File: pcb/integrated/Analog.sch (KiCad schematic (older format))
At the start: 49 parts, among them J5001 Conn_Coaxial, U5001 74LVC1G3157GW, U5002 TLV3501AIDBVR, U5003 74LVC1G3157GW, U5004 MCP6561-OT

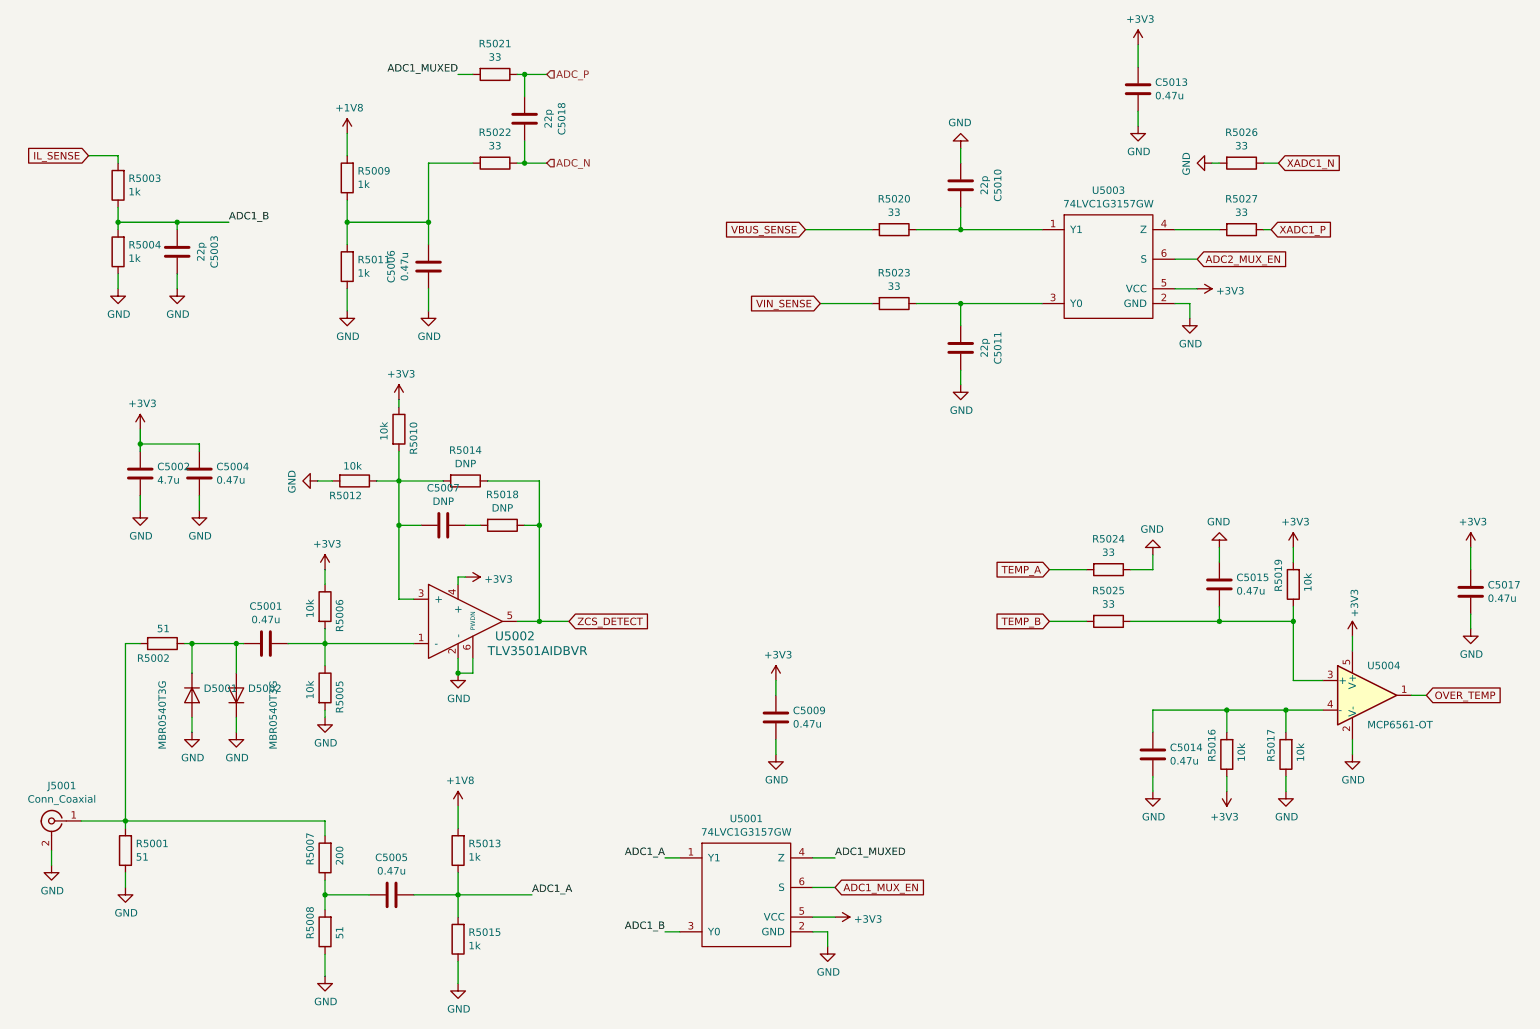
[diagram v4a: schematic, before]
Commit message: updated component values for schematic
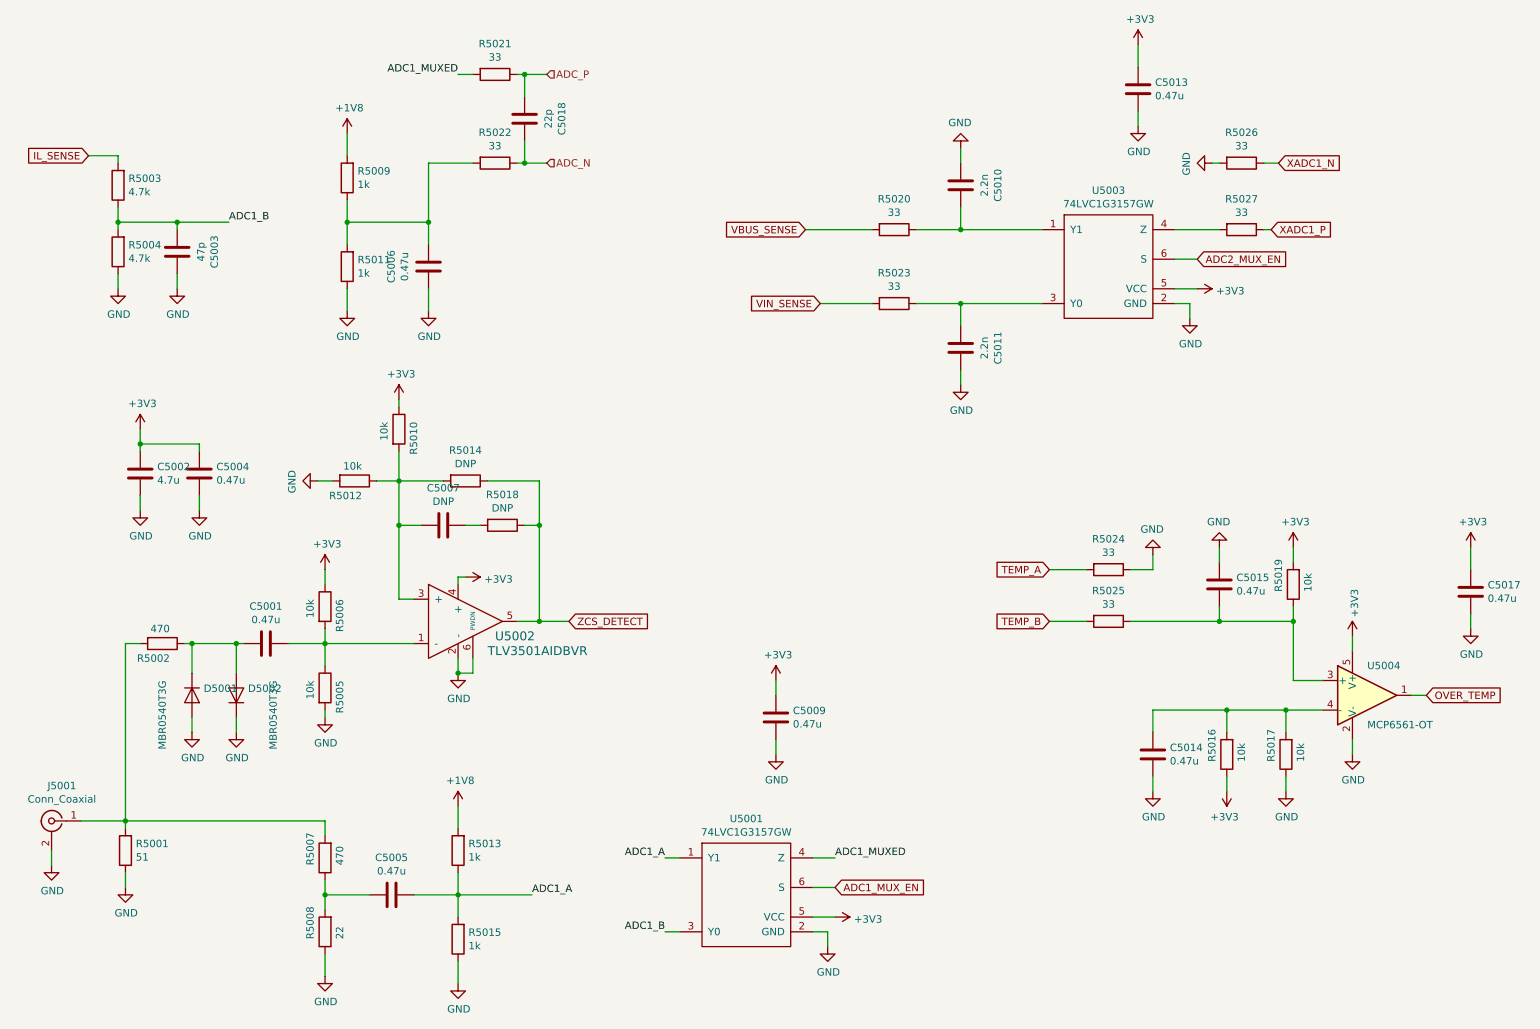
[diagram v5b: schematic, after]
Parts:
- C5003: value 22p -> 47p
- C5010, C5011: value 22p -> 2.2n
- R5002: value 51 -> 470
- R5003, R5004: value 1k -> 4.7k
- R5007: value 200 -> 470
- R5008: value 51 -> 22
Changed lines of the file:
@@
 EESchema Schematic File Version 4
 LIBS:integrated-cache
-EELAYER 30 0
+EELAYER 26 0
 EELAYER END
 $Descr A4 11693 8268
@@
 P 1650 5200
 F 0 "R5002" V 1750 5250 50  0000 R CNN
-F 1 "51" V 1550 5250 50  0000 R CNN
+F 1 "470" V 1550 5250 50  0000 R CNN
 F 2 "Resistor_SMD:R_1206_3216Metric" V 1580 5200 50  0001 C CNN
 F 3 "~" H 1650 5200 50  0001 C CNN
@@
 P 2750 6650
 F 0 "R5007" V 2850 6700 50  0000 R CNN
-F 1 "200" V 2650 6700 50  0000 R CNN
+F 1 "470" V 2650 6700 50  0000 R CNN
 F 2 "Resistor_SMD:R_1206_3216Metric" V 2680 6650 50  0001 C CNN
 F 3 "~" H 2750 6650 50  0001 C CNN
@@
 P 2750 7150
 F 0 "R5008" V 2850 7200 50  0000 R CNN
-F 1 "51" V 2650 7200 50  0000 R CNN
+F 1 "22" V 2650 7200 50  0000 R CNN
 F 2 "Resistor_SMD:R_1206_3216Metric" V 2680 7150 50  0001 C CNN
 F 3 "~" H 2750 7150 50  0001 C CNN
@@
 P 1350 2100
 F 0 "R5003" H 1280 2054 50  0000 R CNN
-F 1 "1k" H 1280 2145 50  0000 R CNN
+F 1 "4.7k" H 1280 2145 50  0000 R CNN
 F 2 "Resistor_SMD:R_0402_1005Metric" V 1280 2100 50  0001 C CNN
 F 3 "~" H 1350 2100 50  0001 C CNN
@@
 P 1350 2550
 F 0 "R5004" H 1280 2504 50  0000 R CNN
-F 1 "1k" H 1280 2595 50  0000 R CNN
+F 1 "4.7k" H 1280 2595 50  0000 R CNN
 F 2 "Resistor_SMD:R_0402_1005Metric" V 1280 2550 50  0001 C CNN
 F 3 "~" H 1350 2550 50  0001 C CNN
@@
 P 1750 2550
 F 0 "C5003" V 1498 2550 50  0000 C CNN
-F 1 "22p" V 1589 2550 50  0000 C CNN
+F 1 "47p" V 1589 2550 50  0000 C CNN
 F 2 "Capacitor_SMD:C_0402_1005Metric" H 1788 2400 50  0001 C CNN
 F 3 "~" H 1750 2550 50  0001 C CNN
@@
 P 7050 2100
 F 0 "C5010" V 6798 2100 50  0000 C CNN
-F 1 "22p" V 6889 2100 50  0000 C CNN
+F 1 "2.2n" V 6889 2100 50  0000 C CNN
 F 2 "Capacitor_SMD:C_0402_1005Metric" H 7088 1950 50  0001 C CNN
 F 3 "~" H 7050 2100 50  0001 C CNN
@@
 P 7050 3200
 F 0 "C5011" V 6798 3200 50  0000 C CNN
-F 1 "22p" V 6889 3200 50  0000 C CNN
+F 1 "2.2n" V 6889 3200 50  0000 C CNN
 F 2 "Capacitor_SMD:C_0402_1005Metric" H 7088 3050 50  0001 C CNN
 F 3 "~" H 7050 3200 50  0001 C CNN
